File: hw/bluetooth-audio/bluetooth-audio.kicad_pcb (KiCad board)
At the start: 4 copper layers, 32.4 x 55.2 mm, 100 parts, among them J1 AudioJack4_Ground, J2 USB_C_Receptacle_USB2.0, J3 Conn_01x06, J4 2x5 JTAG header, Q1 UMH3N, U1 ESP32D0WD-V3, U2 CH340K, U3 TLV71318PDBV, U4 ES8388, U5 USBLC6-2SC6, U6 W25Q32JVZP, U7 NCP1117-3.3_SOT223, Y1 Crystal 40 MHz 10pF

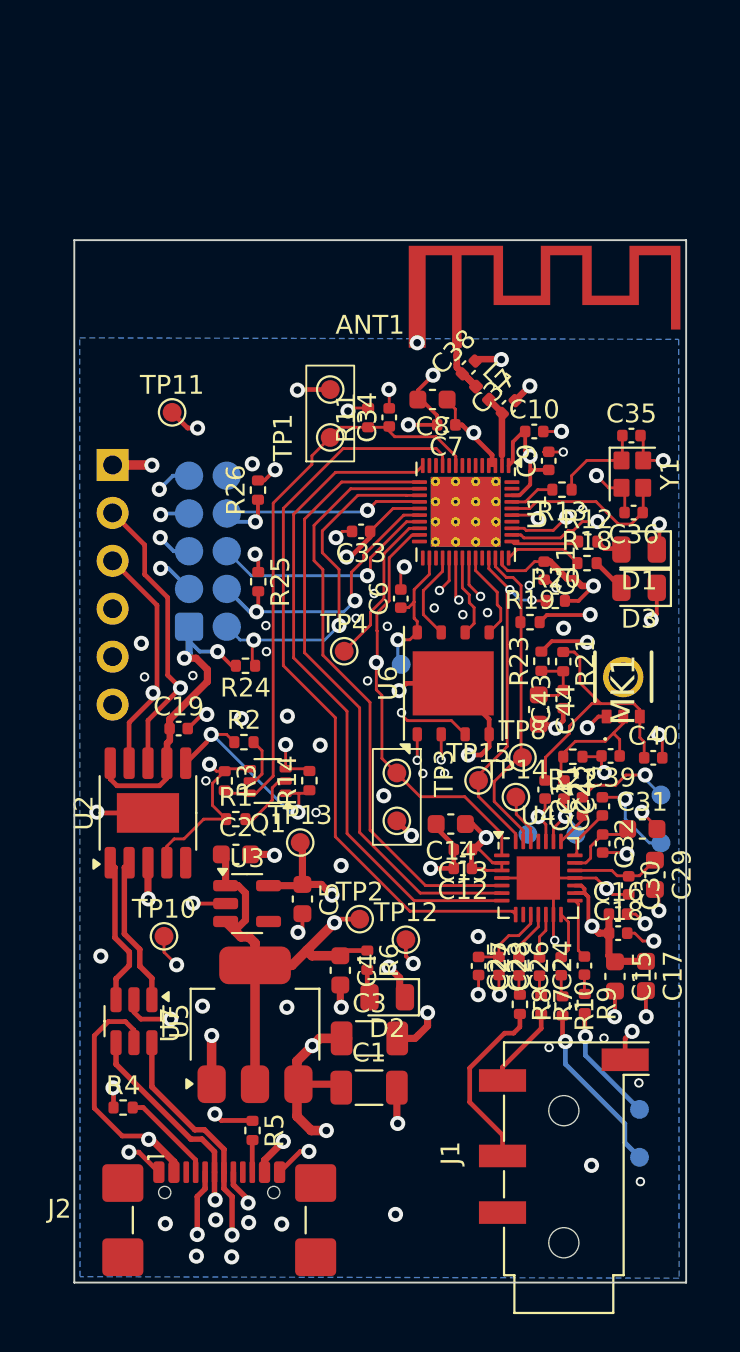
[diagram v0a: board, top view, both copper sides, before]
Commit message: Custom symbol and footprints for IS2083. Updated design document. Initial dump of components onto cleared PCB.
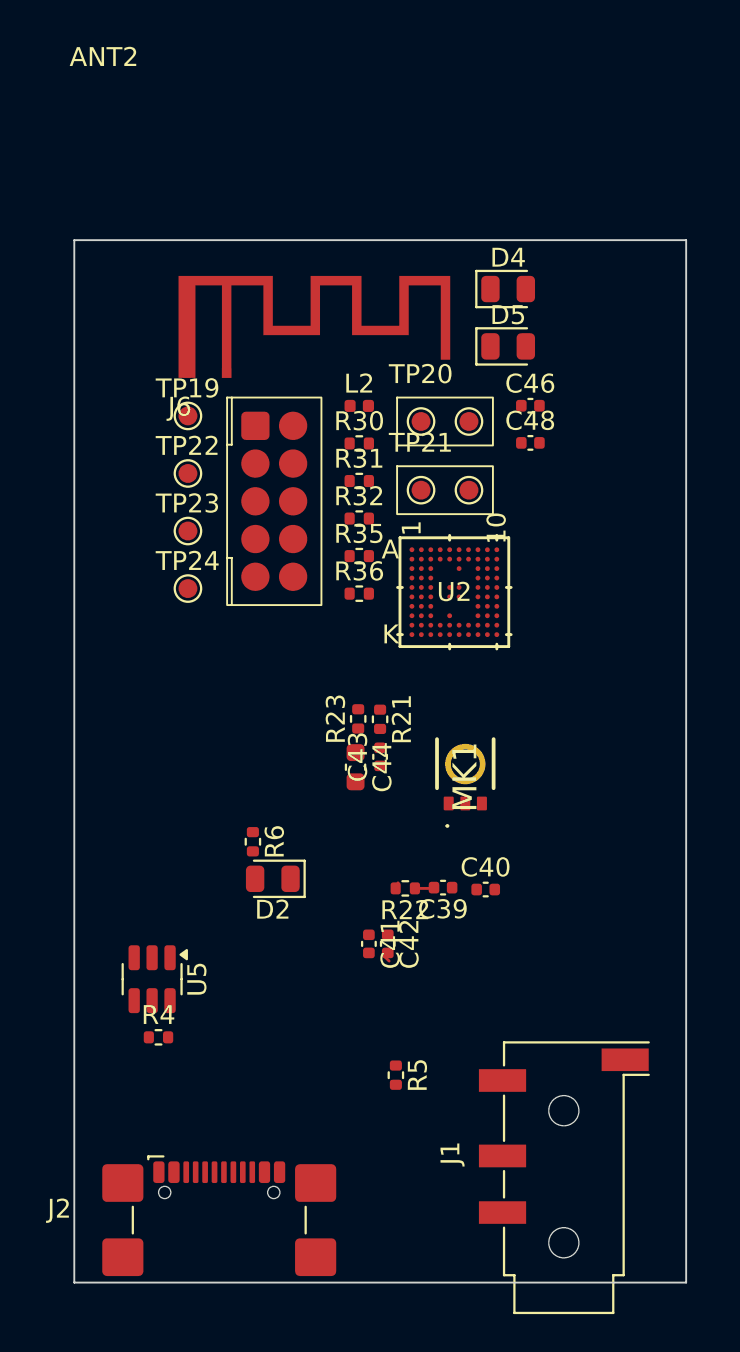
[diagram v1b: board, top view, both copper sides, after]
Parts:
- removed ANT1: 2.4 GHz, custom_footprints:Antenna 2.4GHz Inverted-F Meandered
- removed C1: 1uF, Capacitor_SMD:C_1206_3216Metric
- removed C10, C11, C12, C13, C16, C18, C19, C28, C30, C32, C33, C9: 100nF, Capacitor_SMD:C_0402_1005Metric
- removed C14, C15, C17, C29, C31: 10u, Capacitor_SMD:C_0603_1608Metric
- removed C2, C4, C5: 1uF, Capacitor_SMD:C_0603_1608Metric
- removed C21, C22, C23, C24, C25, C26, C34, C6, C7: 1uF, Capacitor_SMD:C_0402_1005Metric
- removed C27: 10u, Capacitor_SMD:C_0402_1005Metric
- removed C3: 10uF, Capacitor_SMD:C_1206_3216Metric
- removed C35, C36: 18pF, Capacitor_SMD:C_0402_1005Metric
- removed C37, C38: 3.3pF, Capacitor_SMD:C_0402_1005Metric
- removed C8: 10uF, Capacitor_SMD:C_0603_1608Metric
- removed D1: LED_BLUE, LED_SMD:LED_0805_2012Metric
- removed D3: LED_GREEN, LED_SMD:LED_0805_2012Metric
- removed J3: Conn_01x06, Connector_PinHeader_2.54mm:PinHeader_1x06_P2.54mm_Vertical
- removed J4: 2x5 JTAG header, custom_footprints:2x5 2mm JTAG header pads only
- removed L1: 2.2nH, Inductor_SMD:L_0402_1005Metric
- removed Q1: UMH3N, Package_TO_SOT_SMD:SOT-363_SC-70-6
- removed R1, R11, R2: 10k, Resistor_SMD:R_0402_1005Metric
- removed R10, R7, R8, R9: 10R, Resistor_SMD:R_0402_1005Metric
- removed R12, R18: 1k, Resistor_SMD:R_0402_1005Metric
- removed R13, R14, R3: 0R, Resistor_SMD:R_0402_1005Metric
- removed R19, R20, R24, R25, R26: 4k7, Resistor_SMD:R_0402_1005Metric
- removed TP1: TEST_EN, custom_footprints:TestPoint_Pad_2x1_D1.0mm
- removed TP10, TP11, TP12: TEST_GND, TestPoint:TestPoint_Pad_D1.0mm
- removed TP13: TEST_1V8, TestPoint:TestPoint_Pad_D1.0mm
- removed TP14: TEST_I2C_AD, TestPoint:TestPoint_Pad_D1.0mm
- removed TP15: TEST_I2C_CLK, TestPoint:TestPoint_Pad_D1.0mm
- removed TP2: TEST_3V3, TestPoint:TestPoint_Pad_D1.0mm
- removed TP3: TEST_BOOT, custom_footprints:TestPoint_Pad_2x1_D1.0mm
- removed TP4: TEST_GPIO2, TestPoint:TestPoint_Pad_D1.0mm
- removed TP5: TEST_IN_2, custom_footprints:TestPoint_Pad_2x1_D1.0mm
- removed TP6: TEST_OUT_2, custom_footprints:TestPoint_Pad_2x1_D1.0mm
- removed TP7: TEST_MIC_1, custom_footprints:TestPoint_Pad_2x1_D1.0mm
- removed TP8: TEST_I2C_DATA, TestPoint:TestPoint_Pad_D1.0mm
- removed TP9: TEST_VDD_SDIO, TestPoint:TestPoint_Pad_D1.0mm
- removed U1: ESP32D0WD-V3, Package_DFN_QFN:QFN-48-1EP_5x5mm_P0.35mm_EP3.7x3.7mm_ThermalVias
- removed U3: TLV71318PDBV, Package_TO_SOT_SMD:SOT-23-5
- removed U4: ES8388, Package_DFN_QFN:QFN-28-1EP_4x4mm_P0.4mm_EP2.3x2.3mm
- removed U6: W25Q32JVZP, Package_SON:WSON-8-1EP_6x5mm_P1.27mm_EP3.4x4.3mm
- removed U7: NCP1117-3.3_SOT223, Package_TO_SOT_SMD:SOT-223-3_TabPin2
- removed Y1: Crystal 40 MHz 10pF, Crystal:Crystal_SMD_SeikoEpson_FA128-4Pin_2.0x1.6mm
- added ANT2: 2.4 GHz, custom_footprints:Antenna 2.4GHz Inverted-F Meandered, F.Cu at (151.2, 74.4)
- added C46: 3.3pF, Capacitor_SMD:C_0402_1005Metric, F.Cu at (169.9, 76.3)
- added C48: 3.3pF, Capacitor_SMD:C_0402_1005Metric, F.Cu at (169.9, 78.3)
- added D4: LED_BLUE, LED_SMD:LED_0805_2012Metric, F.Cu at (168.7, 70.2)
- added D5: LED_GREEN, LED_SMD:LED_0805_2012Metric, F.Cu at (168.7, 73.2)
- added J6: 2x5 JTAG header, custom_footprints:2x5 2mm JTAG header pads only, F.Cu at (155.3, 77.4)
- added L2: 2.2nH, Inductor_SMD:L_0402_1005Metric, F.Cu at (160.8, 76.3)
- added R30: 4k7, Resistor_SMD:R_0402_1005Metric, F.Cu at (160.8, 78.3)
- added R31: 4k7, Resistor_SMD:R_0402_1005Metric, F.Cu at (160.8, 80.3)
- added R32: 4k7, Resistor_SMD:R_0402_1005Metric, F.Cu at (160.8, 82.3)
- added R35: 1k, Resistor_SMD:R_0402_1005Metric, F.Cu at (160.8, 84.3)
- added R36: 1k, Resistor_SMD:R_0402_1005Metric, F.Cu at (160.8, 86.3)
- added TP19: TEST_GPIO2, TestPoint:TestPoint_Pad_D1.0mm, F.Cu at (151.7, 76.9)
- added TP20: TEST_EN, custom_footprints:TestPoint_Pad_2x1_D1.0mm, F.Cu at (164.1, 77.2)
- added TP21: TEST_BOOT, custom_footprints:TestPoint_Pad_2x1_D1.0mm, F.Cu at (164.1, 80.8)
- added TP22: TEST_GND, TestPoint:TestPoint_Pad_D1.0mm, F.Cu at (151.7, 79.9)
- added TP23: TEST_GND, TestPoint:TestPoint_Pad_D1.0mm, F.Cu at (151.7, 83.0)
- added TP24: TEST_GND, TestPoint:TestPoint_Pad_D1.0mm, F.Cu at (151.7, 86.0)
- U2: value CH340K -> IS2083BM-232; footprint Package_SO:SSOP-10-1EP_3.9x4.9mm_P1mm_EP2.1x3.3mm -> custom_footprints:VFBGA82_3MX_MCH
- moved U2 20.0 mm to (165.8, 86.2), turned to 0 degrees
- moved C41 12.4 mm to (161.3, 104.9)
- moved C42 12.4 mm to (162.3, 104.9)
- moved C40 11.3 mm to (167.5, 102.0)
- moved R22 11.3 mm to (163.2, 101.9)
- moved C39 11.3 mm to (165.2, 101.9)
- moved C43 10.2 mm to (161.9, 94.9)
- moved C44 10.2 mm to (160.6, 95.5)
- moved R21 10.2 mm to (161.9, 93.0)
- moved R23 10.2 mm to (160.7, 92.9)
- moved MK1 9.56 mm to (166.4, 96.0)
- moved D2 8.73 mm to (156.2, 101.4)
- moved R6 8.73 mm to (155.2, 99.4)
- moved R5 8.15 mm to (162.7, 111.8)
- moved R4 4.17 mm to (150.2, 109.8)
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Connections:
- MK1 pad 1: +3V3 -> /audio/AVDD
- R23 pad 2: +3V3 -> /audio/AVDD
- R6 pad 1: +3V3 -> /Power/USB_VBUS
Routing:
- net +3V3: track 181.8 -> 0.00 mm, vias 15 -> 0
- net GND: track 109.2 -> 1.04 mm, vias 100 -> 0
- net /Micro/UART_RX: track 45.0 -> 0.00 mm, vias 2 -> 0
- net /Micro/UART_TX: track 42.9 -> 0.00 mm, vias 2 -> 0
- net ASDOUT: track 40.3 -> 0.00 mm
- net LRCK: track 35.7 -> 0.00 mm
- net DSDIN: track 33.6 -> 0.00 mm
- net SCLK: track 32.0 -> 0.00 mm
- net MCLK: track 31.5 -> 0.00 mm, vias 2 -> 0
- net /Micro/EN: track 30.2 -> 0.00 mm
- net /Power/USB_VBUS: track 25.6 -> 0.00 mm, vias 4 -> 0
- net /Micro/RTS: track 24.2 -> 0.00 mm, vias 2 -> 0
- net +1V8: track 22.8 -> 0.00 mm, vias 2 -> 0
- net I2C_CLK: track 19.1 -> 0.00 mm, vias 2 -> 0
- net /Micro/MTMS: track 19.1 -> 0.00 mm, vias 2 -> 0
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- removed copper zone on In2.Cu, net /Power/USB_VBUS
- removed copper zone on B.Cu, net GND
- removed copper zone on In1.Cu, net GND
- removed copper zone on In2.Cu, net GND

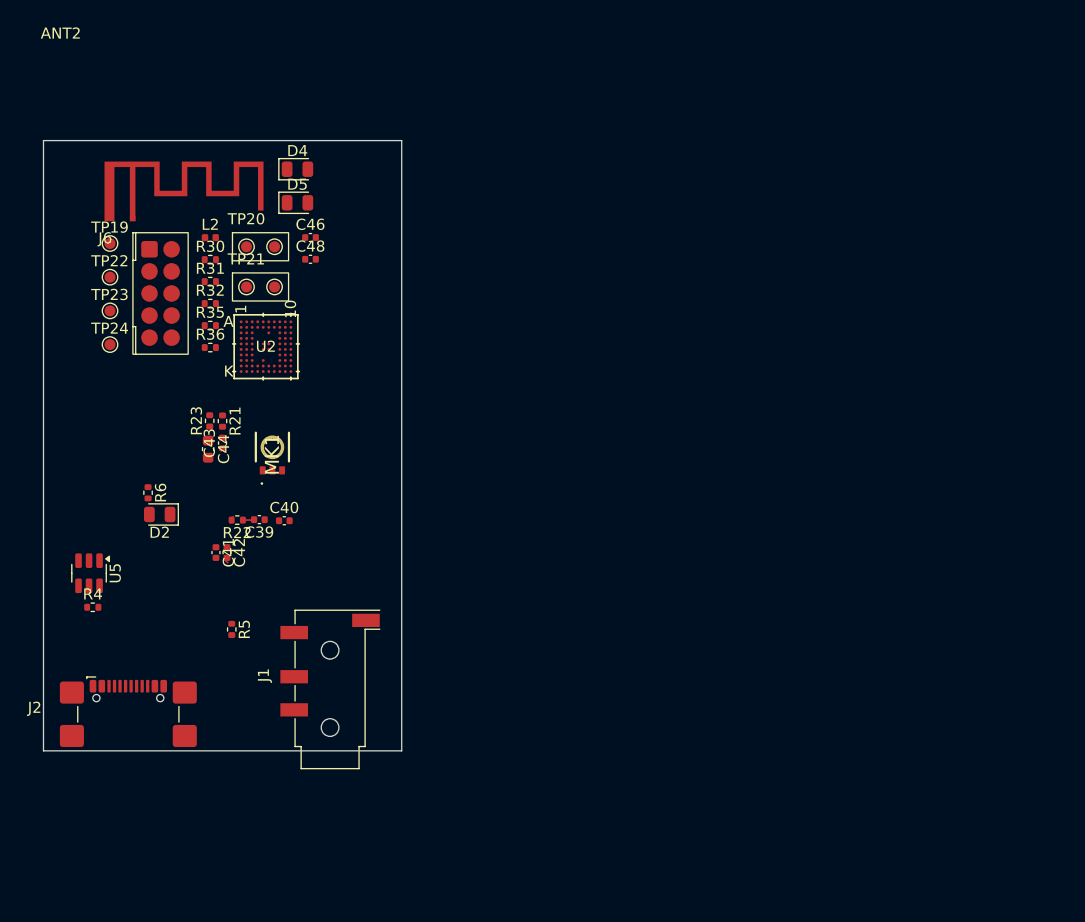
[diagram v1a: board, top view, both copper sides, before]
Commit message: Fixing sheet titles
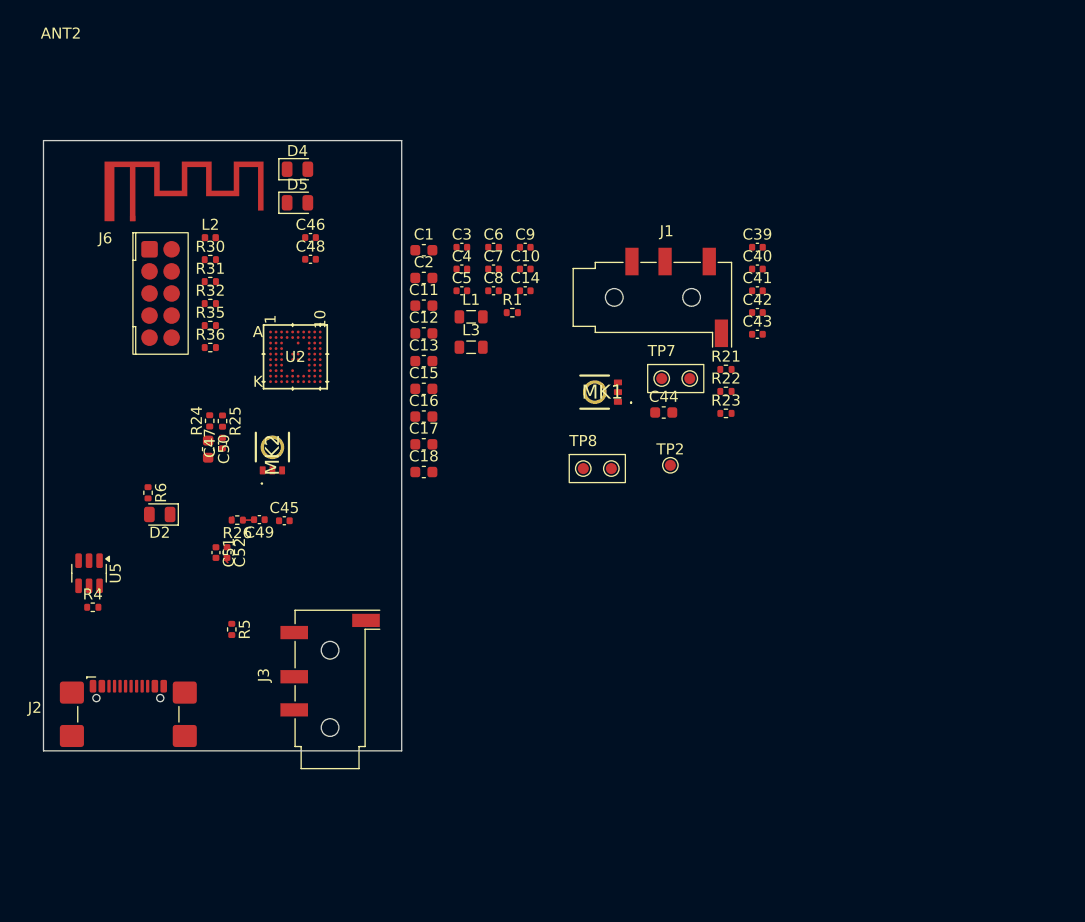
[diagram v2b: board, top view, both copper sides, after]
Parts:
- removed TP19: TEST_GPIO2, TestPoint:TestPoint_Pad_D1.0mm
- removed TP20: TEST_EN, custom_footprints:TestPoint_Pad_2x1_D1.0mm
- removed TP21: TEST_BOOT, custom_footprints:TestPoint_Pad_2x1_D1.0mm
- removed TP22, TP23, TP24: TEST_GND, TestPoint:TestPoint_Pad_D1.0mm
- added C1: 10uF 6.3V, Capacitor_SMD:C_0603_1608Metric, F.Cu at (180.1, 77.5)
- added C10: 1uF, Capacitor_SMD:C_0402_1005Metric, F.Cu at (189.3, 79.2)
- added C11: 1uF 16V, Capacitor_SMD:C_0603_1608Metric, F.Cu at (180.1, 82.5)
- added C12: 1uF 16V, Capacitor_SMD:C_0603_1608Metric, F.Cu at (180.1, 85.0)
- added C13: 1uF 16V, Capacitor_SMD:C_0603_1608Metric, F.Cu at (180.1, 87.5)
- added C14: 1uF, Capacitor_SMD:C_0402_1005Metric, F.Cu at (189.3, 81.2)
- added C15: 1uF 16V, Capacitor_SMD:C_0603_1608Metric, F.Cu at (180.1, 90.0)
- added C16: 10uF 10V, Capacitor_SMD:C_0603_1608Metric, F.Cu at (180.1, 92.5)
- added C17: 1uF 16V, Capacitor_SMD:C_0603_1608Metric, F.Cu at (180.1, 95.1)
- added C18: 1uF 16V, Capacitor_SMD:C_0603_1608Metric, F.Cu at (180.1, 97.6)
- added C2: 10uF 6.3V, Capacitor_SMD:C_0603_1608Metric, F.Cu at (180.1, 80.0)
- added C3: 1uF 16V, Capacitor_SMD:C_0402_1005Metric, F.Cu at (183.6, 77.2)
- added C39: 10nF, Capacitor_SMD:C_0402_1005Metric, F.Cu at (210.3, 77.2)
- added C4: 1uF, Capacitor_SMD:C_0402_1005Metric, F.Cu at (183.6, 79.2)
- added C40: 10nF, Capacitor_SMD:C_0402_1005Metric, F.Cu at (210.3, 79.2)
- added C41: 100nF, Capacitor_SMD:C_0402_1005Metric, F.Cu at (210.3, 81.2)
- added C42: 100nF, Capacitor_SMD:C_0402_1005Metric, F.Cu at (210.3, 83.1)
- added C43: 100nF, Capacitor_SMD:C_0402_1005Metric, F.Cu at (210.3, 85.1)
- added C44: 10u, Capacitor_SMD:C_0603_1608Metric, F.Cu at (201.8, 92.2)
- added C5: 1uF, Capacitor_SMD:C_0402_1005Metric, F.Cu at (183.6, 81.2)
- added C6: 1uF, Capacitor_SMD:C_0402_1005Metric, F.Cu at (186.4, 77.2)
- added C7: 1uF, Capacitor_SMD:C_0402_1005Metric, F.Cu at (186.4, 79.2)
- added C8: 1uF, Capacitor_SMD:C_0402_1005Metric, F.Cu at (186.4, 81.2)
- added C9: 1uF, Capacitor_SMD:C_0402_1005Metric, F.Cu at (189.3, 77.2)
- added J1: AudioJack4_Ground, Connector_Audio:Jack_3.5mm_KoreanHropartsElec_PJ-320D-4A_Horizontal, F.Cu at (202.1, 81.8)
- added L1: 10uH, Inductor_SMD:L_0805_2012Metric, F.Cu at (184.4, 83.5)
- added L3: 10uH, Inductor_SMD:L_0805_2012Metric, F.Cu at (184.4, 86.3)
- added MK1: ICS-40720, custom_footprints:ICS40720, F.Cu at (196.3, 90.3)
- added R1: 1k, Resistor_SMD:R_0402_1005Metric, F.Cu at (188.1, 83.1)
- added R21: 2k2, Resistor_SMD:R_0402_1005Metric, F.Cu at (207.5, 88.3)
- added R22: 2k2, Resistor_SMD:R_0402_1005Metric, F.Cu at (207.5, 90.3)
- added R23: 1k, Resistor_SMD:R_0402_1005Metric, F.Cu at (207.5, 92.3)
- added TP2: TEST_3V3, TestPoint:TestPoint_Pad_D1.0mm, F.Cu at (202.4, 97.0)
- added TP7: TEST_MIC_1, custom_footprints:TestPoint_Pad_2x1_D1.0mm, F.Cu at (201.7, 89.1)
- added TP8: TEST_MIC_1, custom_footprints:TestPoint_Pad_2x1_D1.0mm, F.Cu at (194.6, 97.3)
- moved U2 2.81 mm to (168.5, 87.1)
- renumbered C40 to C45, C43 to C47, C39 to C49, C44 to C50, C41 to C51, C42 to C52, J1 to J3, MK1 to MK2, R23 to R24, R21 to R25, R22 to R26
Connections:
- U2 pad A10: unconnected-(U2B-VCC_RF-PadA10) -> VCC_RF
- U2 pad A2: unconnected-(U2A-AOHPL-PadA2) -> AOHPL
- U2 pad A4: unconnected-(U2B-VDDA_CODEC-PadA4) -> BK2_O_1V8
- U2 pad A5: unconnected-(U2A-AOHPR-PadA5) -> AOHPR
- U2 pad A6: unconnected-(U2A-PA1OP-PadA6) -> /Digital (page 5)/PA1OP
- U2 pad A7: unconnected-(U2B-GND-PadA7) -> GND
- U2 pad A8: unconnected-(U2A-RTX-PadA8) -> /Digital (page 5)/RTX
- U2 pad A9: unconnected-(U2B-VCC_BTPA-PadA9) -> BK1_O_1V5
- U2 pad B10: unconnected-(U2A-XO_P-PadB10) -> XO_P
- U2 pad B2: unconnected-(U2A-SCLK1-PadB2) -> SCLK1
- U2 pad B3: unconnected-(U2A-RFS1-PadB3) -> RFS1
- U2 pad B4: unconnected-(U2B-VCOM-PadB4) -> Net-(U2B-VCOM)
- U2 pad B5: unconnected-(U2A-P1_3/TCK_CPU/SDA-PadB5) -> P1_3
- U2 pad B6: unconnected-(U2A-P1_2/TDI_CPU/SCL-PadB6) -> P1_2
- U2 pad B7: unconnected-(U2B-VCC_PA1-PadB7) -> BK1_O_1V5
- U2 pad B8: unconnected-(U2A-P0_1-PadB8) -> FFWD
- U2 pad C1: unconnected-(U2A-MIC_N1-PadC1) -> MIC_N1
- U2 pad C10: unconnected-(U2A-XO_N-PadC10) -> XO_N
- U2 pad C2: unconnected-(U2A-DT1-PadC2) -> DT1
- U2 pad C8: unconnected-(U2B-VDD_IO-PadC8) -> /Digital (page 5)/VDD_IO
- U2 pad D1: unconnected-(U2A-MIC_P1-PadD1) -> MIC_P1
- U2 pad D10: unconnected-(U2B-ULPC_VSUS-PadD10) -> Net-(U2B-ULPC_VSUS)
- U2 pad D2: unconnected-(U2A-MCLK1-PadD2) -> MCLK1
- U2 pad D3: unconnected-(U2B-VDD_IO-PadD3) -> /Digital (page 5)/VDD_IO
- U2 pad D8: unconnected-(U2A-RST_N-PadD8) -> RST_N
- U2 pad D9: unconnected-(U2A-P0_5-PadD9) -> VOL_DOWN
- U2 pad E1: unconnected-(U2B-MICBIAS-PadE1) -> MIC_BIAS
- U2 pad E10: unconnected-(U2B-VBG-PadE10) -> Net-(U2B-VBG)
- U2 pad E2: unconnected-(U2A-DMIC_CLK-PadE2) -> DMIC_CLK
- U2 pad E3: unconnected-(U2A-DMIC1_L-PadE3) -> DMIC1_L
- U2 pad E5: unconnected-(U2B-GND-PadE5) -> GND
- U2 pad E8: unconnected-(U2A-P0_2-PadE8) -> PLAY_PAUSE
- U2 pad E9: unconnected-(U2A-P2_7-PadE9) -> VOL_UP
- U2 pad F1: unconnected-(U2B-ADAP_IN-PadF1) -> ADAP_IN
- U2 pad F10: unconnected-(U2B-RFLDO_O-PadF10) -> VCC_RF
- U2 pad F2: unconnected-(U2A-DMIC1_R-PadF2) -> DMIC1_R
- U2 pad F3: unconnected-(U2A-AIR-PadF3) -> AIR
- U2 pad F5: unconnected-(U2B-GND-PadF5) -> GND
- U2 pad F6: unconnected-(U2B-GND-PadF6) -> GND
- U2 pad F8: unconnected-(U2A-P0_0/UART_TX_IND-PadF8) -> P0_0
- U2 pad G1: unconnected-(U2B-BAT_IN-PadG1) -> +3V3
- U2 pad G10: unconnected-(U2B-PMIC_IN-PadG10) -> BK1_O_1V5
- U2 pad G2: unconnected-(U2A-P3_2-PadG2) -> P3_2
- U2 pad G3: unconnected-(U2A-AIL-PadG3) -> AIL
- U2 pad G8: unconnected-(U2B-USB_1V2/VDD_CORE-PadG8) -> +1V2
- U2 pad H1: unconnected-(U2B-SARVDD-PadH1) -> BK2_O_1V8
- U2 pad H10: unconnected-(U2B-CLDO_O/VDD_PLL-PadH10) -> +1V2
- U2 pad H2: unconnected-(U2A-P0_6-PadH2) -> P0_6
- U2 pad H3: unconnected-(U2A-P2_6-PadH3) -> P2_6
- U2 pad H5: unconnected-(U2B-VDD_CORE-PadH5) -> +1V2
- U2 pad H8: unconnected-(U2B-AVDD_USB/VDD_IO_10-PadH8) -> LDO_31_VO
- U2 pad H9: unconnected-(U2A-P3_7/UART_CTS-PadH9) -> P3_7
- U2 pad J1: unconnected-(U2B-SYS_POWER-PadJ1) -> SYS_POWER
- U2 pad J10: unconnected-(U2A-USB_DP-PadJ10) -> USB_D+
- U2 pad J2: unconnected-(U2A-P8_6/UART_RXD-PadJ2) -> HCI_RXD
- U2 pad J3: unconnected-(U2A-P8_5/UART_TXD-PadJ3) -> HCI_TXD
- U2 pad J4: unconnected-(U2A-SK1-PadJ4) -> /Digital (page 5)/SK1_AMB_DET
- U2 pad J6: unconnected-(U2B-VDD_CORE-PadJ6) -> +1V2
- U2 pad J7: unconnected-(U2A-P3_4/UART_RTS-PadJ7) -> P3_4
- U2 pad J8: unconnected-(U2A-LED1-PadJ8) -> LED1
- U2 pad J9: unconnected-(U2A-LED2-PadJ9) -> LED2
- U2 pad K1: unconnected-(U2B-BK1_VDDC-PadK1) -> /Digital (page 5)/SYS_PWR
- U2 pad K10: unconnected-(U2A-USB_DM-PadK10) -> USB_D-
- U2 pad K2: unconnected-(U2B-BK1_LX1-PadK2) -> /Digital (page 5)/BK1_LX
- U2 pad K3: unconnected-(U2A-BK1_VOUT-PadK3) -> BK1_O_1V5
- U2 pad K4: unconnected-(U2A-MFB-PadK4) -> /Digital (page 5)/MFB
- U2 pad K5: unconnected-(U2B-LDO31_VO-PadK5) -> LDO_31_VO
- U2 pad K6: unconnected-(U2B-LDO31_VIN-PadK6) -> SYS_POWER
- U2 pad K7: unconnected-(U2A-BK2_VOUT-PadK7) -> BK2_O_1V8
- U2 pad K8: unconnected-(U2B-BK2_LX-PadK8) -> /Digital (page 5)/BK2_LX
- U2 pad K9: unconnected-(U2B-BK2_VDD-PadK9) -> /Digital (page 5)/SYS_PWR

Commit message: TODO diff
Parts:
- removed C39, C40: 10nF, Capacitor_SMD:C_0402_1005Metric
- removed C41, C42, C43: 100nF, Capacitor_SMD:C_0402_1005Metric
- removed C44: 10u, Capacitor_SMD:C_0603_1608Metric
- removed MK1: ICS-40720, custom_footprints:ICS40720
- removed R21, R22: 2k2, Resistor_SMD:R_0402_1005Metric
- removed R23: 1k, Resistor_SMD:R_0402_1005Metric
- removed TP7: TEST_MIC_1, custom_footprints:TestPoint_Pad_2x1_D1.0mm
- added C19: 10uF 16V, Capacitor_SMD:C_0603_1608Metric, F.Cu at (202.3, 135.7)
- J1: value AudioJack4_Ground -> 3008TR; footprint Connector_Audio:Jack_3.5mm_KoreanHropartsElec_PJ-320D-4A_Horizontal -> Battery:BatteryHolder_Keystone_3008_1x2450
- moved J1 43.1 mm to (219.7, 121.2)
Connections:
- net /Digital (page 5)/BK1_LX renamed /Digital/BK1_LX
- net /Digital (page 5)/BK2_LX renamed /Digital/BK2_LX
- net /Digital (page 5)/LED_BLUE renamed /Digital/LED_BLUE
- net /Digital (page 5)/LED_GREEN renamed /Digital/LED_GREEN
- net /Digital (page 5)/MFB renamed /Digital/MFB
- net /Digital (page 5)/MTCK renamed /Digital/MTCK
- net /Digital (page 5)/MTDI renamed /Digital/MTDI
- net /Digital (page 5)/MTDO renamed /Digital/MTDO
- net /Digital (page 5)/MTMS renamed /Digital/MTMS
- net /Digital (page 5)/PA1OP renamed /Digital/PA1OP
- net /Digital (page 5)/RTX renamed /Digital/RTX
- net /Digital (page 5)/SK1_AMB_DET renamed /Digital/SK1_AMB_DET
- net /Digital (page 5)/SYS_PWR renamed /Digital/SYS_PWR
- net /Digital (page 5)/VDD_IO renamed /Digital/VDD_IO
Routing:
- net unconnected-(U2A-AOHPM-PadA3): track 0.00 -> 1.59 mm
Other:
- board size 32.4 x 55.2 mm -> 67.2 x 55.2 mm
